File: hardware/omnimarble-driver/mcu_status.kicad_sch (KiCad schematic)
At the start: 11 parts, among them J10 PICO-SOCKET, J11 IO-BREAKOUT, J9 PICO-SOCKET, Q4 MMBT3904

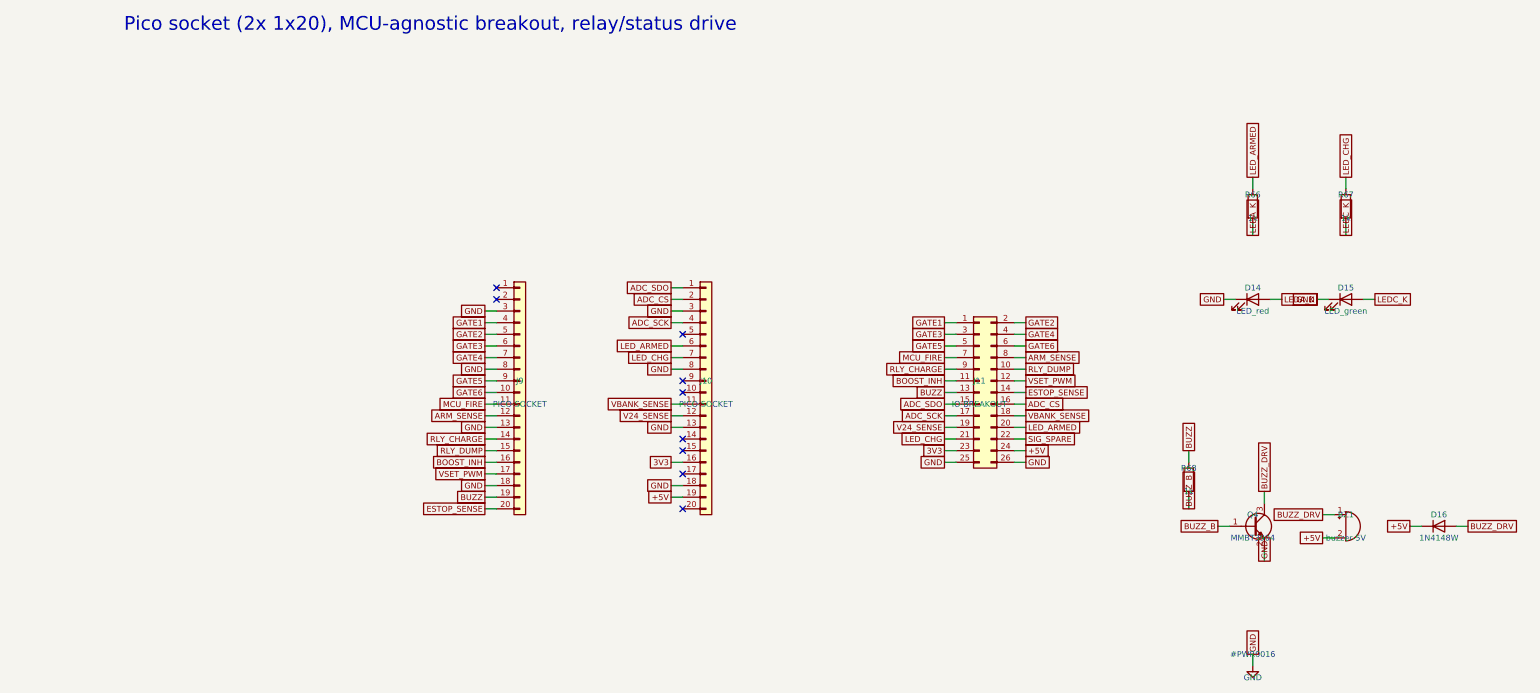
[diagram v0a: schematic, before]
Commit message: Address external design review: boost FB + OVP redesign, BOM freeze
Review findings accepted and fixed (each verified by machine check):

1. Boost feedback network was wrong (confirmed: as-drawn spanned
   54-68V with PWM inverted vs the comment). Redesigned: RT/RB/RJ =
   100k/10k/9.1k with the exact transfer function documented in the
   schematic and design-calcs.md. PWM=0 (MCU-dead state) commands
   55.0V; full PWM commands 18.7V (below the 24.5V converter floor).
   New calcs.py asserts both endpoints.
2. OVP tripped at 55.6V, not the claimed 63V (confirmed). Redesigned:
   CJ431 (+/-0.5%) + 100k/4.3k 1% -> 60.5V nominal, 59.1-62.0V across
   tolerances. Protection ladder asserted in calcs.py: 55V operating
   < 59.1V trip-min, 62.0V trip-max < 63V cap rating - 1V. Operating
   ceiling deliberately reduced 60->55V to keep the bands disjoint.
3. BOM/schematic controller split-brain: bom.csv was stale
   (pre-UC3843 swap); regenerated from parts.py. Both now UC3843B.
4. High-power placeholders now real orderable parts (LCSC-verified):
   47R/5W SQM cement C5807995, dump redesigned to 2x 100R/10W cement
   in series C216413 (no 20-25W part stocked on LCSC; 5.3s to <5V),
   50mR/3W 2512 C2994645, 63V/35V electrolytics C28241/C176666, 10uH
   Sunlord C79272, MINI fuses+Keystone 3568 holders, buzzer, Pico
   sockets/breakout headers. Single documented exception: the 6.8k/2W
   bleed (CRH2512J6K80E04Z) is marked ORDER-REVIEW because LCSC's
   search is uncrawlable - validate.py allowlists it visibly.
5. validate.py pulled forward from the fab phase: fails on unknown
   footprints, blank LCSC on machine-placed parts, missing Variant
   fields, and duplicate refs; generates per-variant gate-rail BOMs
   (bom_rail_emit/recv.csv). Caught two bad footprint names.
6. Paralleling constraints now on the schematic (same-lot FETs,
   symmetric copper, <25mm gate loops, driver return at shunt star).
7. Fail-safe defaults hardened: MCU_FIRE and FIRE_GATED get explicit
   pulldow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
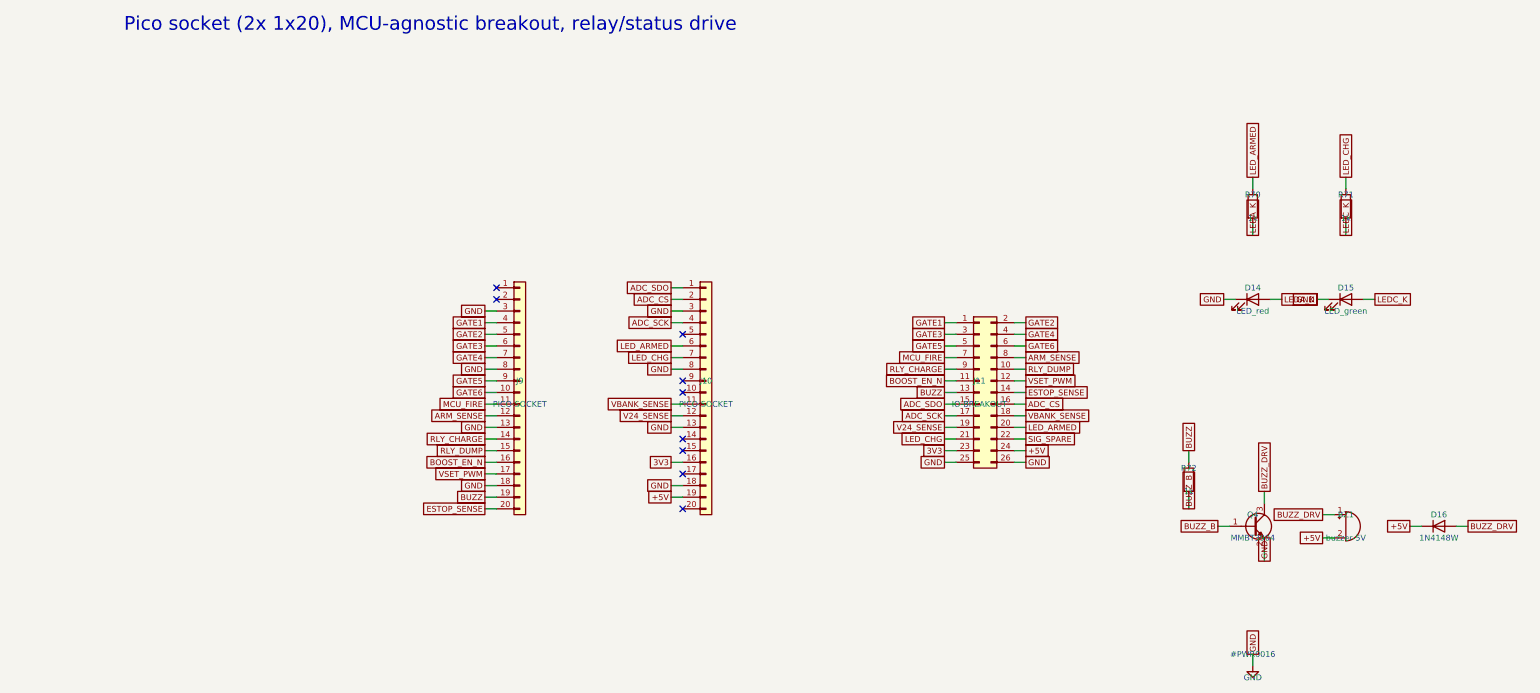
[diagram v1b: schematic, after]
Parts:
- removed R66, R67, R68: 1k, Resistor_SMD:R_0603_1608Metric, symbol Device:R
- added R70, R71, R72: 1k, Resistor_SMD:R_0603_1608Metric, symbol Device:R
- BZ1: LCSC (none) -> C409842
- J10, J9: LCSC (none) -> C50984
- J11: LCSC (none) -> C124383
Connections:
- net BUZZ: now also R72.1
- net BUZZ_B: now also R72.2
- net LEDA_K: now also R70.2
- net LEDC_K: now also R71.2
- net LED_ARMED: now also R70.1
- net LED_CHG: now also R71.1
- net BOOST_INH renamed BOOST_EN_N
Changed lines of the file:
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@@
+			)
+		)
+		(property "LCSC" "C50984"
+			(at 49.53 100.33 0)
+			(show_name no)
+			(do_not_autoplace no)
+			(hide yes)
+			(effects
+				(font
+					(size 1.27 1.27)
+				)
 			)
 		)
@@
 		(instances
 			(project "omnimarble-driver"
-				(path "/73d8eff6-39f1-4e5f-a80b-a36699d4dd7c/9a6b881e-de96-4d92-be5d-8c154f59e0f5"
+				(path "/324ed851-0be4-493c-900d-5ec8847c0520/18efb47f-e397-43d5-a9d6-03f0933f749e"
 					(reference "J9")
 					(unit 1)
@@
 		)
 	)
-	(global_label "BOOST_INH"
+	(global_label "BOOST_EN_N"
 		(shape passive)
 		(at 41.91 115.57 180)
@@
 			)
 		)
+		(property "LCSC" "C50984"
+			(at 90.17 100.33 0)
+			(show_name no)
+			(do_not_autoplace no)
+			(hide yes)
+			(effects
+				(font
+					(size 1.27 1.27)
+				)
+			)
+		)
 		(pin "1"
 		)
@@
 		(instances
 			(project "omnimarble-driver"
-				(path "/73d8eff6-39f1-4e5f-a80b-a36699d4dd7c/9a6b881e-de96-4d92-be5d-8c154f59e0f5"
+				(path "/324ed851-0be4-493c-900d-5ec8847c0520/18efb47f-e397-43d5-a9d6-03f0933f749e"
 					(reference "J10")
 					(unit 1)
@@
 			)
 		)
+		(property "LCSC" "C124383"
+			(at 149.86 100.33 0)
+			(show_name no)
+			(do_not_autoplace no)
+			(hide yes)
+			(effects
+				(font
+					(size 1.27 1.27)
+				)
+			)
+		)
 		(pin "1"
 		)
@@
 		(instances
 			(project "omnimarble-driver"
-				(path "/73d8eff6-39f1-4e5f-a80b-a36699d4dd7c/9a6b881e-de96-4d92-be5d-8c154f59e0f5"
+				(path "/324ed851-0be4-493c-900d-5ec8847c0520/18efb47f-e397-43d5-a9d6-03f0933f749e"
 					(reference "J11")
 					(unit 1)
@@
 		)
 	)
-	(global_label "BOOST_INH"
+	(global_label "BOOST_EN_N"
 		(shape passive)
 		(at 142.24 97.79 180)
@@
 		(on_board yes)
 		(dnp no)
-		(property "Reference" "R66"
+		(property "Reference" "R70"
 			(at 209.55 57.15 0)
 			(show_name no)
@@
 		(instances
 			(project "omnimarble-driver"
-				(path "/73d8eff6-39f1-4e5f-a80b-a36699d4dd7c/9a6b881e-de96-4d92-be5d-8c154f59e0f5"
-					(reference "R66")
+				(path "/324ed851-0be4-493c-900d-5ec8847c0520/18efb47f-e397-43d5-a9d6-03f0933f749e"
+					(reference "R70")
 					(unit 1)
 				)
@@
 		(instances
 			(project "omnimarble-driver"
-				(path "/73d8eff6-39f1-4e5f-a80b-a36699d4dd7c/9a6b881e-de96-4d92-be5d-8c154f59e0f5"
+				(path "/324ed851-0be4-493c-900d-5ec8847c0520/18efb47f-e397-43d5-a9d6-03f0933f749e"
 					(reference "D14")
 					(unit 1)
@@
 		(on_board yes)
 		(dnp no)
-		(property "Reference" "R67"
+		(property "Reference" "R71"
 			(at 229.87 57.15 0)
 			(show_name no)
@@
 		(instances
 			(project "omnimarble-driver"
-				(path "/73d8eff6-39f1-4e5f-a80b-a36699d4dd7c/9a6b881e-de96-4d92-be5d-8c154f59e0f5"
-					(reference "R67")
+				(path "/324ed851-0be4-493c-900d-5ec8847c0520/18efb47f-e397-43d5-a9d6-03f0933f749e"
+					(reference "R71")
 					(unit 1)
 				)
@@
 		(instances
 			(project "omnimarble-driver"
-				(path "/73d8eff6-39f1-4e5f-a80b-a36699d4dd7c/9a6b881e-de96-4d92-be5d-8c154f59e0f5"
+				(path "/324ed851-0be4-493c-900d-5ec8847c0520/18efb47f-e397-43d5-a9d6-03f0933f749e"
 					(reference "D15")
 					(unit 1)
@@
 		(instances
 			(project "omnimarble-driver"
-				(path "/73d8eff6-39f1-4e5f-a80b-a36699d4dd7c/9a6b881e-de96-4d92-be5d-8c154f59e0f5"
+				(path "/324ed851-0be4-493c-900d-5ec8847c0520/18efb47f-e397-43d5-a9d6-03f0933f749e"
 					(reference "Q4")
 					(unit 1)
@@
 		(on_board yes)
 		(dnp no)
-		(property "Reference" "R68"
+		(property "Reference" "R72"
 			(at 195.58 116.84 0)
 			(show_name no)
@@
 		(instances
 			(project "omnimarble-driver"
-				(path "/73d8eff6-39f1-4e5f-a80b-a36699d4dd7c/9a6b881e-de96-4d92-be5d-8c154f59e0f5"
-					(reference "R68")
+				(path "/324ed851-0be4-493c-900d-5ec8847c0520/18efb47f-e397-43d5-a9d6-03f0933f749e"
+					(reference "R72")
 					(unit 1)
 				)
@@
 			)
 		)
+		(property "LCSC" "C409842"
+			(at 229.87 129.54 0)
+			(show_name no)
+			(do_not_autoplace no)
+			(hide yes)
+			(effects
+				(font
+					(size 1.27 1.27)
+				)
+			)
+		)
 		(pin "1"
 		)
@@
 		(instances
 			(project "omnimarble-driver"
-				(path "/73d8eff6-39f1-4e5f-a80b-a36699d4dd7c/9a6b881e-de96-4d92-be5d-8c154f59e0f5"
+				(path "/324ed851-0be4-493c-900d-5ec8847c0520/18efb47f-e397-43d5-a9d6-03f0933f749e"
 					(reference "BZ1")
 					(unit 1)
@@
 		(instances
 			(project "omnimarble-driver"
-				(path "/73d8eff6-39f1-4e5f-a80b-a36699d4dd7c/9a6b881e-de96-4d92-be5d-8c154f59e0f5"
+				(path "/324ed851-0be4-493c-900d-5ec8847c0520/18efb47f-e397-43d5-a9d6-03f0933f749e"
 					(reference "D16")
 					(unit 1)
@@
 		(instances
 			(project "omnimarble-driver"
-				(path "/73d8eff6-39f1-4e5f-a80b-a36699d4dd7c/9a6b881e-de96-4d92-be5d-8c154f59e0f5"
+				(path "/324ed851-0be4-493c-900d-5ec8847c0520/18efb47f-e397-43d5-a9d6-03f0933f749e"
 					(reference "#PWR0016")
 					(unit 1)

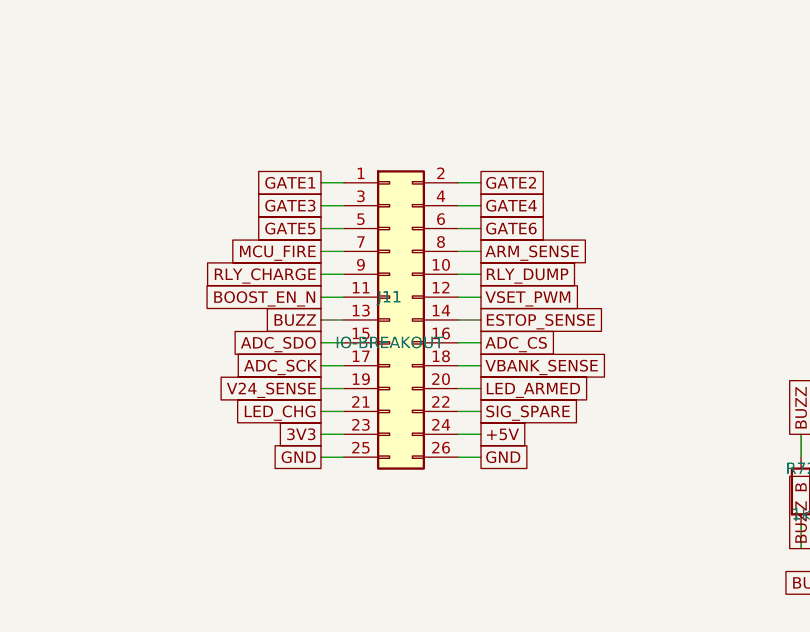
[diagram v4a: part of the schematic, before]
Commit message: Driver PCB: remove J11 IO-breakout + GND-pour tuning (unconnected 11->9)
Per design review: the 2x13 J11 breakout duplicated all 26 control/sense nets
(GATE1-6, MCU_FIRE, ARM/ESTOP, ADC SPI, boost EN/PWM, ...) into the congested
MCU/sense area, doubling the routing burden there. Removed it; MCU-agnostic
access is preserved via the Pico socket pins (J9/J10) for a Pico-form-factor
carrier or jumpers. Netlist drops from 265->241 preroute airwires.

- gen_schematic.py: J11 removed; .kicad_pro now written WITH board design
  rules (min via 0.4 / hole 0.2 / hole-to-hole 0.25) so kicad-cli DRC uses
  them instead of KiCad's stricter defaults after every regen.
- gen_pcb.py build_zones: F/B GND pour clearance 0.3->0.2, min_thick
  0.25->0.13 so the pour flows into narrow necks and reaches isolated GND pads.

Board (220mm, both GND planes): 0 shorts/clearance/parity, 9 unconnected
(2 GND + 3V3 x2 + SW_DRAIN/VBOOST/+24V/BSTINH_B/VSET_PWM), 2 cosmetic
text_height, 1 via_dangling.

Co-Authored-By: Claude Fable 5 <noreply@anthropic.com>
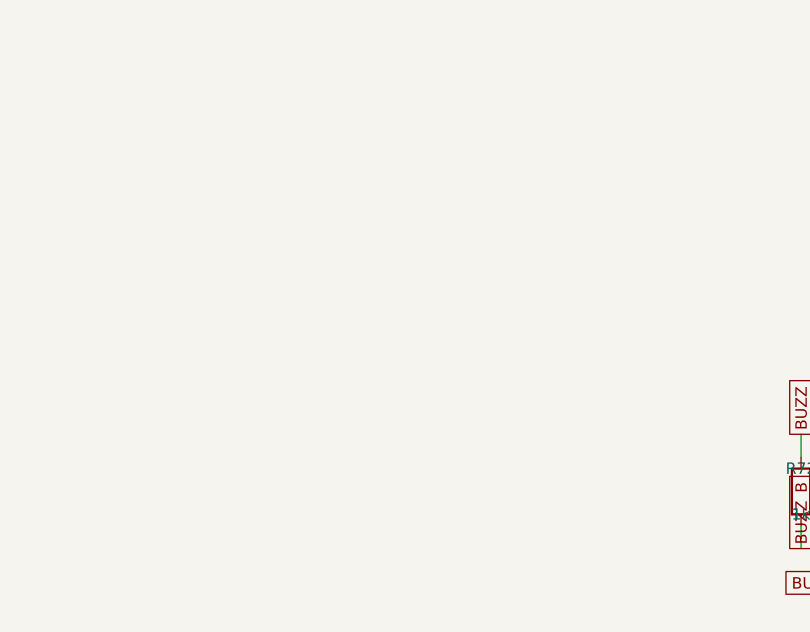
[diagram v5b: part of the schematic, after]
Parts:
- removed J11: IO-BREAKOUT, Connector_PinHeader_2.54mm:PinHeader_2x13_P2.54mm_Vertical, symbol Connector_Generic:Conn_02x13_Odd_Even

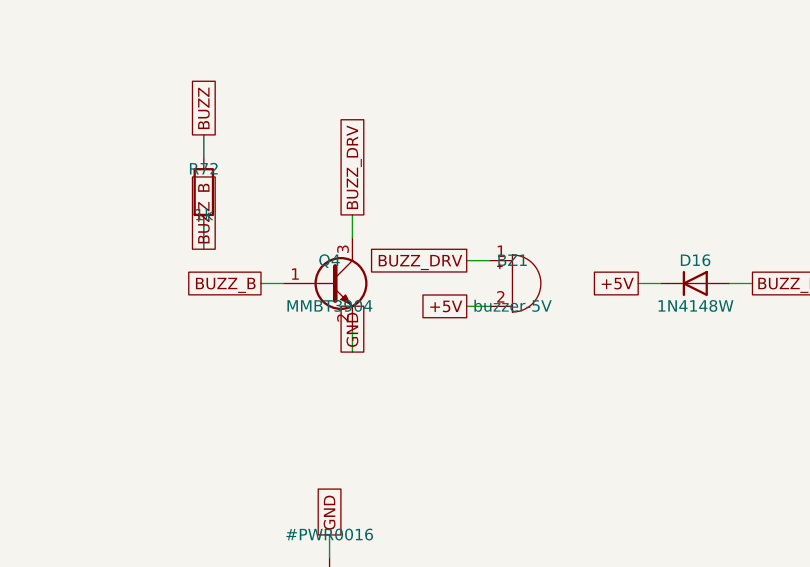
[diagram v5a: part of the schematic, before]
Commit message: Driver PCB: resolve both safety blockers + should-fixes, re-route, DRC-clean
Two datasheet-level blockers (invisible to netlist checks) + the should-fixes
from two review rounds, then a full DeepPCB re-route on the corrected netlist.

Blockers:
- U5 shunt ref: CJ431/C3113 (pinout 1=REF,2=K,3=A) did NOT match the TL431DBZ
  footprint -> OVP dead. Now TL431BIDBZR/C41283 (+/-0.5%, 1=K,2=REF,3=A). Kept
  +/-0.5% grade (the 1% A-grade would blow the 62.0V OVP ceiling).
- Relay HF3FF footprint had NO/NC transposed (datasheet bottom-view copied
  without mirroring) -> dump/charge logic inverted. Swapped pads 12<->14 +
  corrected silk. VERIFY WITH OHMMETER at bring-up (COM-NC @rest) -- parity is
  green by construction, DRC cannot see this.

Should-fixes: D90 SMBJ33A->SMBJ26CA (bidirectional, clamps below AP63205);
snubber 4.7k->4.7Ohm; R7 0.05->0.15Ohm (boost ilim); R25 10k->47k (0.28W->0.06W
LED series); BZ1 polarity swap. 78L12->DPAK deferred (reflows the placement
band; documented, fan-cool for bench per user).

Routing: full DeepPCB re-route from the corrected DSN. dsn_fixup now injects a
B.Cu keepout over the FET-strip corridor so the router can't pack signals where
the SHUNT_HI bus lives (rev-40 dropped the locked bus). import-clean re-authors
the SHUNT_HI B.Cu bus deterministically. Post-import repairs: re-authored the
RS1->NT1 Kelvin tie (DeepPCB routed SHUNT_HI on F.Cu shorting ISNS_P), joined a
MCU_FIRE via gap, bulged GATE6 off a 3V3 via, island-removal + a stitch via to
unify the fragmented F.Cu SHUNT_HI pour.

DRC 0 electrical / 0 unconnected; validate.py --production, validate_widths,
check_netlist, calcs all PASS.

Co-Authored-By: Claude Opus 4.8 <noreply@anthropic.com>
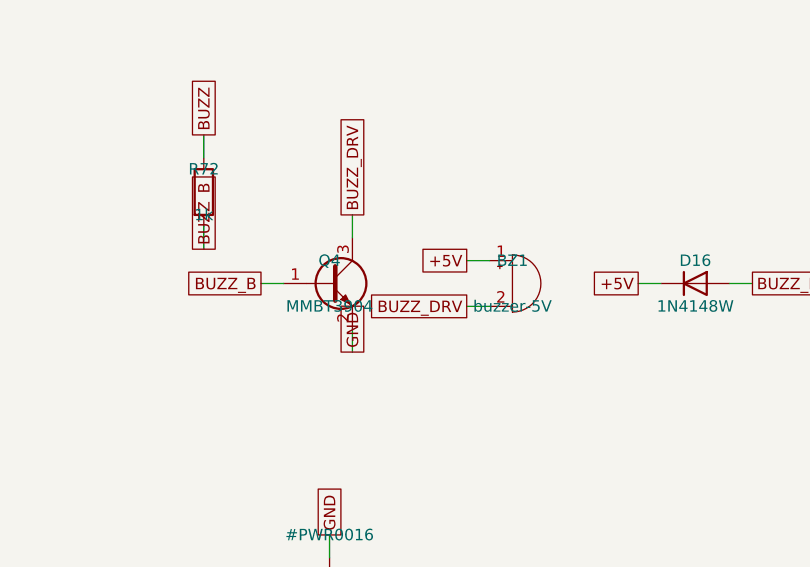
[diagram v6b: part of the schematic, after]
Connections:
- net +5V: now also BZ1.1 (+); no longer BZ1.2 (-)
- net BUZZ_DRV: now also BZ1.2 (-); no longer BZ1.1 (+)
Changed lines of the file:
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@@
 		(instances
 			(project "omnimarble-driver"
-				(path "/3eaa9588-078e-48af-b393-9dad6bd20142/40b2befc-6602-4ef5-87e0-4195a66754a5"
+				(path "/4f6b9534-97fd-44ae-b81e-62754cb6cba6/75f25778-acbd-42b3-9f04-352847a17f55"
 					(reference "J9")
 					(unit 1)
@@
 		(instances
 			(project "omnimarble-driver"
-				(path "/3eaa9588-078e-48af-b393-9dad6bd20142/40b2befc-6602-4ef5-87e0-4195a66754a5"
+				(path "/4f6b9534-97fd-44ae-b81e-62754cb6cba6/75f25778-acbd-42b3-9f04-352847a17f55"
 					(reference "J10")
 					(unit 1)
@@
 		(instances
 			(project "omnimarble-driver"
-				(path "/3eaa9588-078e-48af-b393-9dad6bd20142/40b2befc-6602-4ef5-87e0-4195a66754a5"
+				(path "/4f6b9534-97fd-44ae-b81e-62754cb6cba6/75f25778-acbd-42b3-9f04-352847a17f55"
 					(reference "R70")
 					(unit 1)
@@
 		(instances
 			(project "omnimarble-driver"
-				(path "/3eaa9588-078e-48af-b393-9dad6bd20142/40b2befc-6602-4ef5-87e0-4195a66754a5"
+				(path "/4f6b9534-97fd-44ae-b81e-62754cb6cba6/75f25778-acbd-42b3-9f04-352847a17f55"
 					(reference "D14")
 					(unit 1)
@@
 		(instances
 			(project "omnimarble-driver"
-				(path "/3eaa9588-078e-48af-b393-9dad6bd20142/40b2befc-6602-4ef5-87e0-4195a66754a5"
+				(path "/4f6b9534-97fd-44ae-b81e-62754cb6cba6/75f25778-acbd-42b3-9f04-352847a17f55"
 					(reference "R71")
 					(unit 1)
@@
 		(instances
 			(project "omnimarble-driver"
-				(path "/3eaa9588-078e-48af-b393-9dad6bd20142/40b2befc-6602-4ef5-87e0-4195a66754a5"
+				(path "/4f6b9534-97fd-44ae-b81e-62754cb6cba6/75f25778-acbd-42b3-9f04-352847a17f55"
 					(reference "D15")
 					(unit 1)
@@
 		(instances
 			(project "omnimarble-driver"
-				(path "/3eaa9588-078e-48af-b393-9dad6bd20142/40b2befc-6602-4ef5-87e0-4195a66754a5"
+				(path "/4f6b9534-97fd-44ae-b81e-62754cb6cba6/75f25778-acbd-42b3-9f04-352847a17f55"
 					(reference "Q4")
 					(unit 1)
@@
 		(instances
 			(project "omnimarble-driver"
-				(path "/3eaa9588-078e-48af-b393-9dad6bd20142/40b2befc-6602-4ef5-87e0-4195a66754a5"
+				(path "/4f6b9534-97fd-44ae-b81e-62754cb6cba6/75f25778-acbd-42b3-9f04-352847a17f55"
 					(reference "R72")
 					(unit 1)
@@
 		(instances
 			(project "omnimarble-driver"
-				(path "/3eaa9588-078e-48af-b393-9dad6bd20142/40b2befc-6602-4ef5-87e0-4195a66754a5"
+				(path "/4f6b9534-97fd-44ae-b81e-62754cb6cba6/75f25778-acbd-42b3-9f04-352847a17f55"
 					(reference "BZ1")
 					(unit 1)
@@
 		)
 	)
-	(global_label "BUZZ_DRV"
+	(global_label "+5V"
 		(shape passive)
 		(at 224.79 127 180)
@@
 		)
 	)
-	(global_label "+5V"
+	(global_label "BUZZ_DRV"
 		(shape passive)
 		(at 224.79 132.08 180)
@@
 		(instances
 			(project "omnimarble-driver"
-				(path "/3eaa9588-078e-48af-b393-9dad6bd20142/40b2befc-6602-4ef5-87e0-4195a66754a5"
+				(path "/4f6b9534-97fd-44ae-b81e-62754cb6cba6/75f25778-acbd-42b3-9f04-352847a17f55"
 					(reference "D16")
 					(unit 1)
@@
 		(instances
 			(project "omnimarble-driver"
-				(path "/3eaa9588-078e-48af-b393-9dad6bd20142/40b2befc-6602-4ef5-87e0-4195a66754a5"
+				(path "/4f6b9534-97fd-44ae-b81e-62754cb6cba6/75f25778-acbd-42b3-9f04-352847a17f55"
 					(reference "#PWR0016")
 					(unit 1)
